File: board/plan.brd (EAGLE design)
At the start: 37.5 x 23.5 mm, 14 parts, among them IC1 TINY24/44/84-SSU, X1 250-404, X2 250-408

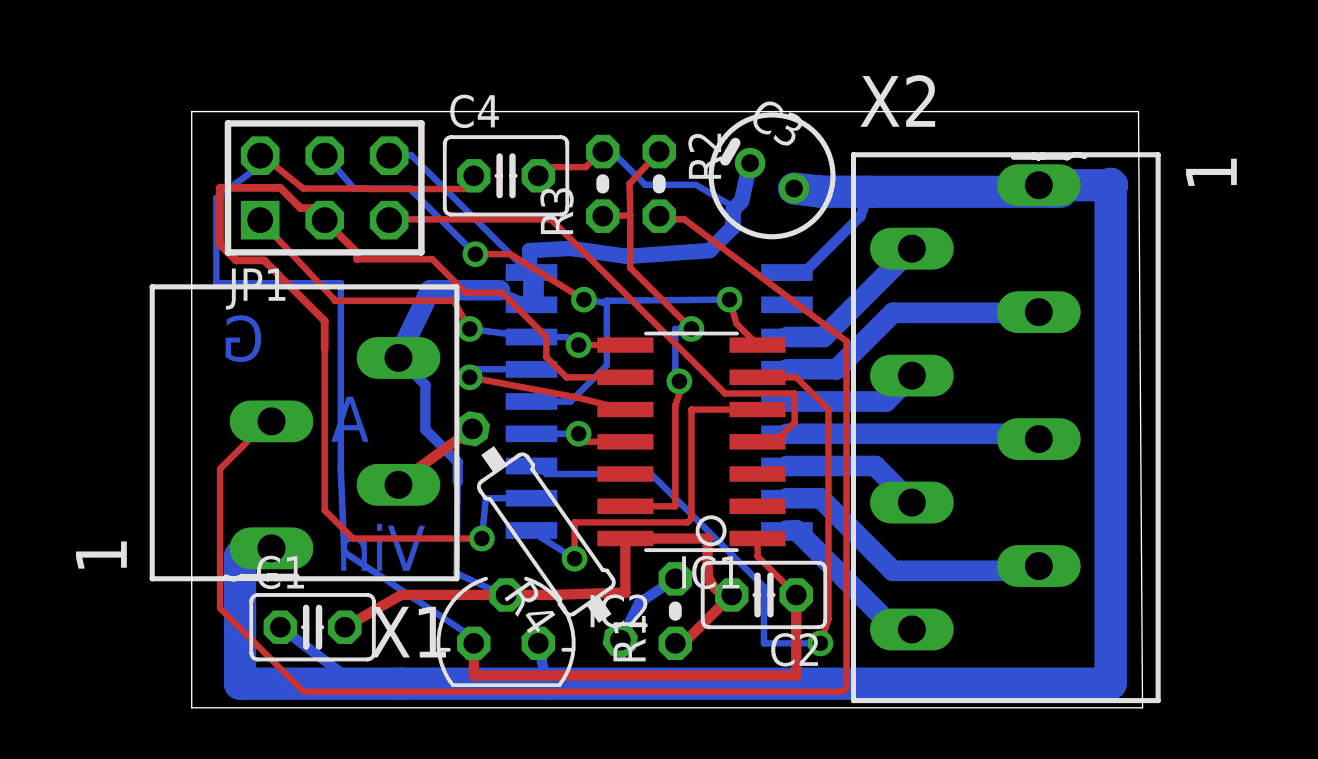
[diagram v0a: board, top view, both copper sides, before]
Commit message: Fixed missing connection to ADC input
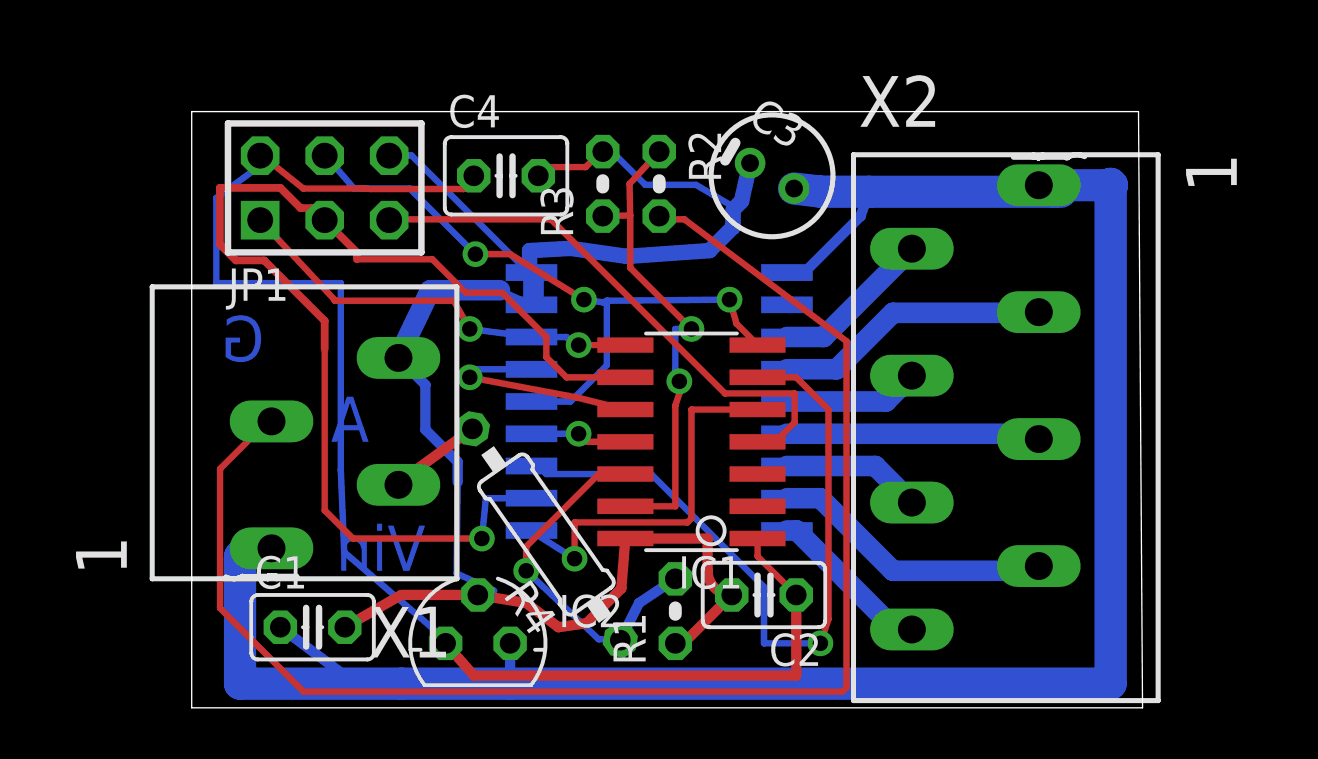
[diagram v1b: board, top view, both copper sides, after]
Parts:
- moved IC2 1.11 mm to (31.0, 35.9)
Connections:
- removed net N$21: IC1.2
- removed net N$9: IC1.3
- net N$18: now also IC1.12
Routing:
- net N$18: track 3.36 -> 14.2 mm, vias 0 -> 1
- net +5V: track 57.5 -> 56.5 mm
- net GND: track 73.2 -> 74.0 mm
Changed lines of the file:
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@@
 <elements>
 <element name="IC1" library="avr-7" package="SOIC14" value="TINY24/44/84-SSU" x="39.37" y="43.815" rot="R90"/>
-<element name="IC2" library="v-reg" package="78LXX" value="" x="32.0675" y="35.8775"/>
+<element name="IC2" library="v-reg" package="78LXX" value="" x="30.95625" y="35.8775"/>
 <element name="C1" library="rcl" package="C025-025X050" value="0.33µ" x="24.4475" y="36.5125"/>
 <element name="C2" library="rcl" package="C025-025X050" value="0.01µ" x="42.2275" y="37.7825" rot="R180"/>
@@
 <wire x1="32.9184" y1="50.5206" x2="33.0708" y2="50.4825" width="0.254" layer="16"/>
 <wire x1="27.48915" y1="55.0926" x2="27.46375" y2="55.08625" width="0.254" layer="16"/>
-<wire x1="32.0675" y1="37.7825" x2="27.94" y2="37.7825" width="0.4064" layer="1"/>
+<wire x1="30.95625" y1="37.7825" x2="27.94" y2="37.7825" width="0.4064" layer="1"/>
 <wire x1="27.94" y1="37.7825" x2="25.7175" y2="36.5125" width="0.4064" layer="1"/>
 <wire x1="33.147" y1="50.292" x2="33.147" y2="49.3776" width="0.8128" layer="16"/>
@@
 <wire x1="30.11805" y1="38.6334" x2="30.1625" y2="42.2275" width="0.254" layer="16"/>
 <wire x1="31.5976" y1="37.9476" x2="30.11805" y2="38.6334" width="0.254" layer="16"/>
-<wire x1="31.5976" y1="37.9476" x2="32.0675" y2="37.7825" width="0.254" layer="16"/>
+<wire x1="31.5976" y1="37.9476" x2="30.95625" y2="37.7825" width="0.254" layer="16"/>
 <contactref element="R1" pad="1"/>
-<wire x1="32.0675" y1="37.7825" x2="33.81375" y2="37.7825" width="0.4064" layer="1"/>
-<wire x1="33.81375" y1="37.7825" x2="36.7665" y2="37.87775" width="0.4064" layer="1"/>
-<wire x1="36.7665" y1="37.87775" x2="36.7665" y2="40.005" width="0.4064" layer="1"/>
+<wire x1="30.95625" y1="37.7825" x2="32.86125" y2="37.465" width="0.4064" layer="1"/>
+<wire x1="36.60775" y1="38.0365" x2="36.7665" y2="40.005" width="0.4064" layer="1"/>
 <wire x1="36.7665" y1="40.005" x2="40.005" y2="40.005" width="0.4064" layer="1"/>
 <wire x1="40.005" y1="40.005" x2="40.005" y2="38.735" width="0.4064" layer="1"/>
@@
 <wire x1="35.8775" y1="55.245" x2="35.56" y2="54.9275" width="0.254" layer="1"/>
 <wire x1="35.56" y1="54.9275" x2="35.52825" y2="54.95925" width="0.254" layer="1"/>
+<wire x1="32.86125" y1="37.465" x2="34.13125" y2="36.5125" width="0.4064" layer="1"/>
+<wire x1="34.13125" y1="36.5125" x2="35.2425" y2="36.67125" width="0.4064" layer="1"/>
+<wire x1="35.2425" y1="36.67125" x2="36.60775" y2="38.0365" width="0.4064" layer="1"/>
 </signal>
 <signal name="+5V">
@@
 <wire x1="20.65655" y1="53.42255" x2="22.3012" y2="54.6354" width="0.254" layer="16"/>
 <wire x1="22.3012" y1="55.0926" x2="22.38375" y2="55.08625" width="0.254" layer="16"/>
-<wire x1="30.7975" y1="35.8775" x2="30.7975" y2="34.6075" width="0.4064" layer="1"/>
+<wire x1="29.68625" y1="35.8775" x2="30.7975" y2="34.6075" width="0.4064" layer="1"/>
 <wire x1="30.7975" y1="34.6075" x2="43.4975" y2="34.6075" width="0.4064" layer="1"/>
 <wire x1="43.4975" y1="34.6075" x2="43.4975" y2="37.7825" width="0.4064" layer="1"/>
@@
 <wire x1="25.55875" y1="42.70375" x2="25.55875" y2="50.0634" width="0.254" layer="16"/>
 <wire x1="25.55875" y1="50.0634" x2="20.65655" y2="50.0634" width="0.254" layer="16"/>
-<wire x1="31.0896" y1="35.8902" x2="25.6921" y2="39.4716" width="0.254" layer="16"/>
-<wire x1="31.0896" y1="35.8902" x2="30.7975" y2="35.8775" width="0.254" layer="16"/>
+<wire x1="29.66085" y1="36.04895" x2="25.6921" y2="39.4716" width="0.254" layer="16"/>
+<wire x1="29.66085" y1="36.04895" x2="29.68625" y2="35.8775" width="0.254" layer="16"/>
 <wire x1="43.4975" y1="37.7825" x2="41.9735" y2="39.3065" width="0.254" layer="1"/>
 <wire x1="41.9735" y1="39.3065" x2="41.9735" y2="40.005" width="0.254" layer="1"/>
@@
 <wire x1="42.9768" y1="50.292" x2="43.1292" y2="50.4825" width="0.254" layer="16"/>
 <wire x1="21.59" y1="34.29" x2="27.94" y2="34.29" width="1.27" layer="16"/>
-<wire x1="27.94" y1="34.29" x2="33.655" y2="34.29" width="1.27" layer="16"/>
-<wire x1="33.655" y1="34.29" x2="55.88" y2="34.29" width="1.27" layer="16"/>
+<wire x1="27.94" y1="34.29" x2="32.22625" y2="34.29" width="1.27" layer="16"/>
+<wire x1="32.22625" y1="34.29" x2="55.88" y2="34.29" width="1.27" layer="16"/>
 <wire x1="55.88" y1="34.29" x2="55.88" y2="53.975" width="1.27" layer="16"/>
 <wire x1="44.45" y1="53.6702" x2="46.36135" y2="53.66385" width="1.27" layer="16"/>
@@
 <wire x1="53.0525" y1="53.9222" x2="53.39915" y2="53.9222" width="1.27" layer="16"/>
 <wire x1="53.39915" y1="53.9222" x2="53.6575" y2="53.66385" width="1.27" layer="16"/>
-<wire x1="33.3375" y1="35.8775" x2="33.655" y2="34.29" width="0.4064" layer="16"/>
+<wire x1="32.22625" y1="35.8775" x2="32.22625" y2="34.29" width="0.4064" layer="16"/>
 <wire x1="23.1775" y1="36.5125" x2="25.7175" y2="34.6075" width="0.4064" layer="16"/>
 <wire x1="25.7175" y1="34.6075" x2="27.94" y2="34.29" width="0.4064" layer="16"/>
@@
 <wire x1="27.48915" y1="52.578" x2="33.8328" y2="52.578" width="0.254" layer="1"/>
 <wire x1="42.0624" y1="43.8912" x2="41.9735" y2="43.815" width="0.254" layer="1"/>
-<wire x1="27.48915" y1="52.578" x2="27.46375" y2="52.54625" width="0" layer="19" extent="1-16"/>
+<wire x1="27.48915" y1="52.578" x2="27.46375" y2="52.54625" width="0" layer="19" extent="1-1"/>
 </signal>
 <signal name="N$3">
@@
 <wire x1="38.735" y1="38.4175" x2="37.30625" y2="37.465" width="0.4064" layer="16"/>
 <wire x1="37.30625" y1="37.465" x2="36.568765625" y2="36.00245625" width="0.4064" layer="16"/>
+<contactref element="IC1" pad="12"/>
+<wire x1="36.7665" y1="42.545" x2="35.71875" y2="42.545" width="0.254" layer="1"/>
+<wire x1="35.71875" y1="42.545" x2="32.86125" y2="39.6875" width="0.254" layer="1"/>
+<wire x1="32.86125" y1="39.6875" x2="32.86125" y2="38.735" width="0.254" layer="1"/>
+<via x="32.86125" y="38.735" extent="1-16" drill="0.6096" shape="square"/>
+<wire x1="32.86125" y1="38.735" x2="35.71875" y2="36.03625" width="0.254" layer="16"/>
+<wire x1="35.71875" y1="36.03625" x2="36.534971875" y2="36.03625" width="0.254" layer="16"/>
+<wire x1="36.534971875" y1="36.03625" x2="36.568765625" y2="36.00245625" width="0.254" layer="16"/>
 </signal>
 <signal name="N$6">
@@
 <wire x1="34.925" y1="44.1325" x2="33.0708" y2="44.1325" width="0.254" layer="16"/>
 </signal>
-<signal name="N$9">
-<contactref element="IC1" pad="3"/>
-</signal>
-<signal name="N$21">
-<contactref element="IC1" pad="2"/>
-</signal>
 </signals>
